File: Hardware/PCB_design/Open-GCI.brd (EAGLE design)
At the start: 100 x 94 mm, 29 parts, among them IC1 IC1, IC2 IC2, X1 USB

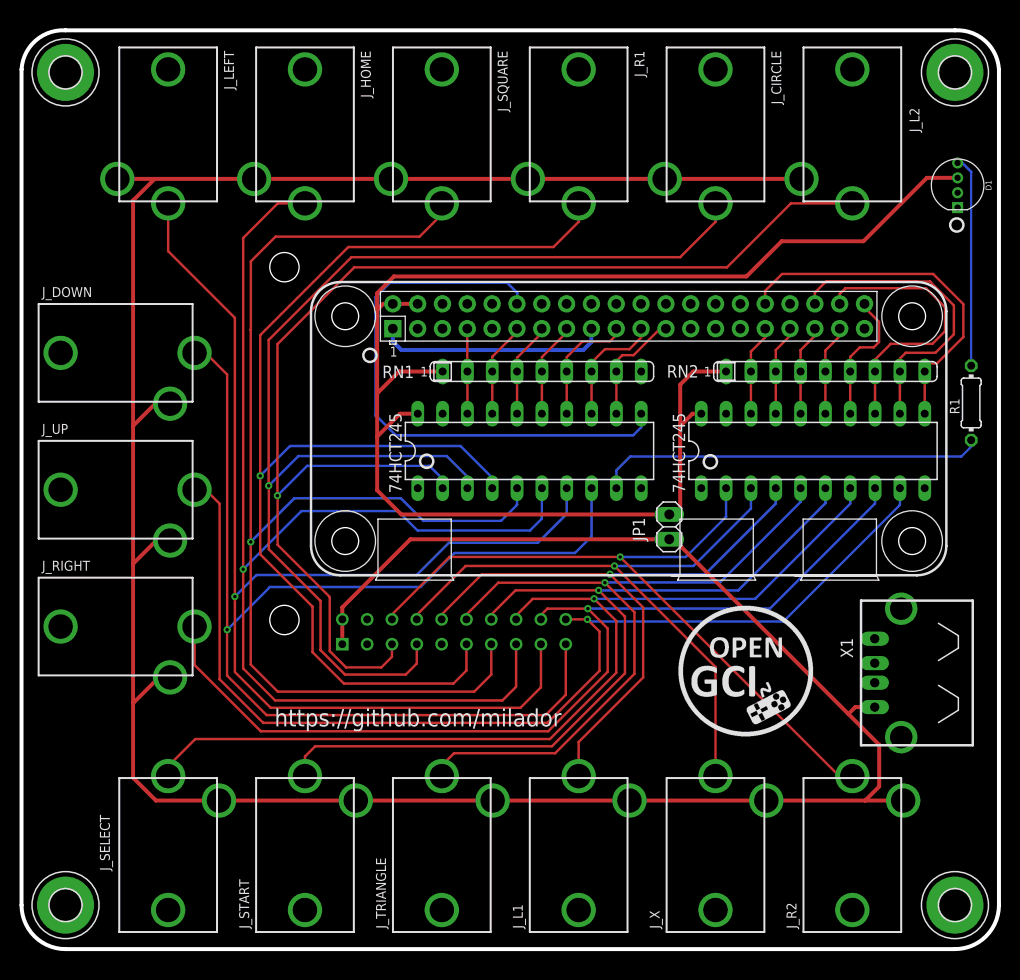
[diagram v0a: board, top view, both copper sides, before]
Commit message: Fixed the 3.5mm jack issue
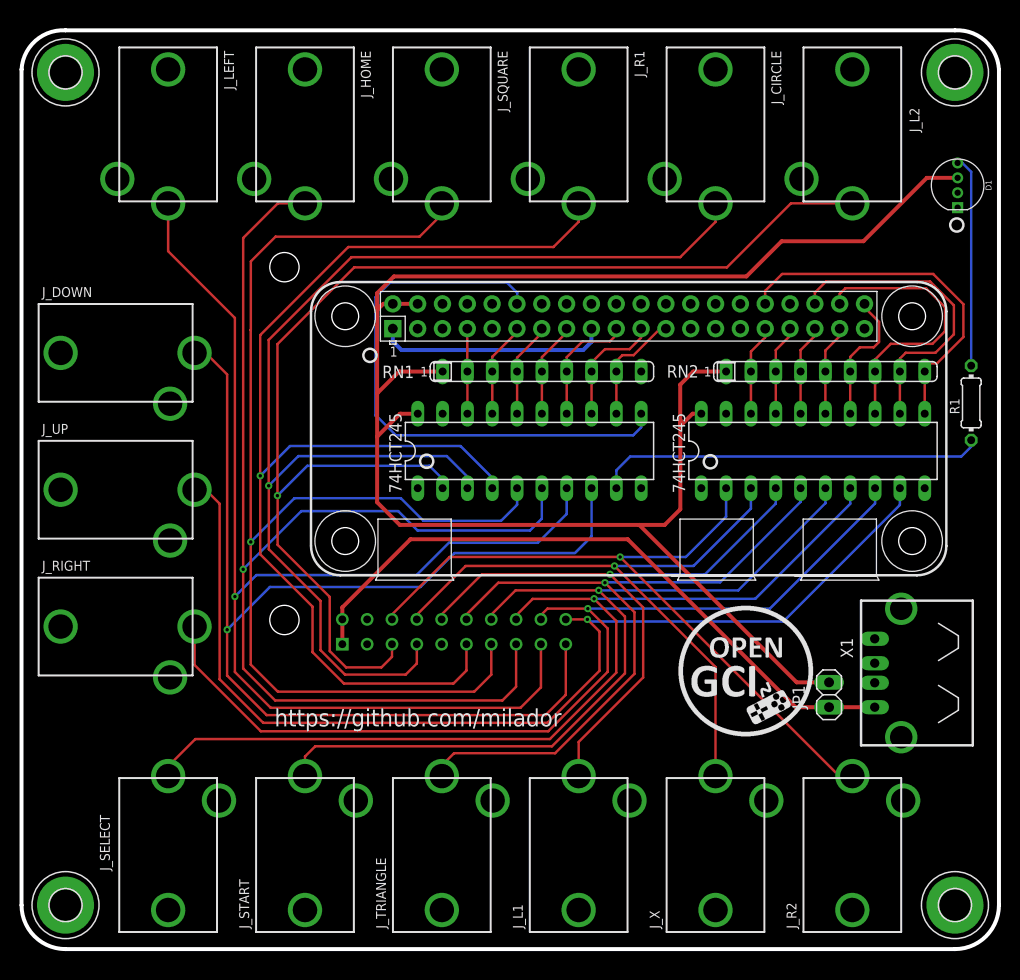
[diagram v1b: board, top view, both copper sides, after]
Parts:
- moved JP1 23.7 mm to (82.6, 26.0)
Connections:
- net +5V/2: no longer J_CIRCLE.3, J_DOWN.3, J_HOME.3, J_L1.3, J_L2.3, J_LEFT.3, J_R1.3, J_R2.3, J_RIGHT.3, J_SELECT.3, J_SQUARE.3, J_START.3, J_TRIANGLE.3, J_UP.3, J_X.3
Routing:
- net +5V/2: track 305.9 -> 68.2 mm
- net +5V: track 154.5 -> 182.9 mm
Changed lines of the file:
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@@
 <setting verticaltext="up"/>
 </settings>
-<grid distance="0.00999999999" unitdist="mm" unit="mm" style="lines" multiple="1" display="yes" altdistance="5" altunitdist="mil" altunit="mil"/>
+<grid distance="0.00196850394" unitdist="inch" unit="inch" style="lines" multiple="1" display="yes" altdistance="5" altunitdist="mil" altunit="mil"/>
 <layers>
 <layer number="1" name="Top" color="4" fill="1" visible="yes" active="yes"/>
@@
 <attribute name="OC_NEWARK" value="unknown" x="82.245" y="59.0945625" size="1.778" layer="27" display="off"/>
 </element>
-<element name="X1" library="open-gci-package" package="PN87520-S" package3d_urn="urn:adsk.eagle:package:6147/1" value="USB" x="90" y="28.255403125" smashed="yes" rot="R90">
-<attribute name="MF" value="" x="90" y="28.255403125" size="1.778" layer="27" rot="R90" display="off"/>
-<attribute name="MPN" value="" x="90" y="28.255403125" size="1.778" layer="27" rot="R90" display="off"/>
-<attribute name="NAME" x="85.07" y="29.775403125" size="1.27" layer="25" rot="R90"/>
-<attribute name="OC_FARNELL" value="unknown" x="90" y="28.255403125" size="1.778" layer="27" rot="R90" display="off"/>
-<attribute name="OC_NEWARK" value="unknown" x="90" y="28.255403125" size="1.778" layer="27" rot="R90" display="off"/>
-<attribute name="VALUE" x="90.980440625" y="30.06134375" size="1.27" layer="27" rot="R270"/>
+<element name="X1" library="open-gci-package" package="PN87520-S" package3d_urn="urn:adsk.eagle:package:6147/1" value="USB" x="90" y="28.25" smashed="yes" rot="R90">
+<attribute name="MF" value="" x="90" y="28.25" size="1.778" layer="27" rot="R90" display="off"/>
+<attribute name="MPN" value="" x="90" y="28.25" size="1.778" layer="27" rot="R90" display="off"/>
+<attribute name="NAME" x="85.07" y="29.77" size="1.27" layer="25" rot="R90"/>
+<attribute name="OC_FARNELL" value="unknown" x="90" y="28.25" size="1.778" layer="27" rot="R90" display="off"/>
+<attribute name="OC_NEWARK" value="unknown" x="90" y="28.25" size="1.778" layer="27" rot="R90" display="off"/>
+<attribute name="VALUE" x="90.980440625" y="30.055940625" size="1.27" layer="27" rot="R270"/>
 </element>
 <element name="D1" library="open-gci-package" package="NEOPIXEL-RGB-THRU" value="RGB LED" x="95.77196875" y="78.14690625" rot="R270"/>
@@
 <attribute name="VALUE" x="96.6774" y="56.8556" size="0.9906" layer="27" ratio="10" rot="R270"/>
 </element>
-<element name="JP1" library="pinhead" library_urn="urn:adsk.eagle:library:325" package="1X02" package3d_urn="urn:adsk.eagle:package:22435/2" value="No Rpi" x="66.27" y="43.2" smashed="yes" rot="R90">
-<attribute name="NAME" x="63.7912" y="41.7538" size="1.27" layer="25" ratio="10" rot="R90"/>
+<element name="JP1" library="pinhead" library_urn="urn:adsk.eagle:library:325" package="1X02" package3d_urn="urn:adsk.eagle:package:22435/2" value="No Rpi" x="82.62" y="26.02" smashed="yes" rot="R90">
+<attribute name="NAME" x="80.1412" y="24.5738" size="1.27" layer="25" ratio="10" rot="R90"/>
 </element>
 </elements>
@@
 <wire x1="36.381690625" y1="67.105528125" x2="36.381690625" y2="65.39103125" width="0.4064" layer="1"/>
 <wire x1="38.09619375" y1="68.82003125" x2="36.381690625" y2="67.105528125" width="0.4064" layer="1"/>
-<wire x1="36.381690625" y1="46.943009375" x2="36.381690625" y2="52.429409375" width="0.4064" layer="1"/>
 <contactref element="JP1" pad="2"/>
-<wire x1="66.27" y1="44.47" x2="38.8547" y2="44.47" width="0.4064" layer="1"/>
-<wire x1="38.8547" y1="44.47" x2="36.381690625" y2="46.943009375" width="0.4064" layer="1"/>
 <wire x1="72.085" y1="59.0945625" x2="68.7345625" y2="59.0945625" width="0.4064" layer="1"/>
 <wire x1="68.7345625" y1="59.0945625" x2="67.39" y2="57.75" width="0.4064" layer="1"/>
-<wire x1="67.39" y1="57.75" x2="67.39" y2="53.52" width="0.4064" layer="1"/>
-<wire x1="67.39" y1="53.52" x2="67.39" y2="45.02" width="0.4064" layer="1"/>
-<wire x1="66.84" y1="44.47" x2="66.27" y2="44.47" width="0.4064" layer="1"/>
-<wire x1="67.39" y1="45.02" x2="66.84" y2="44.47" width="0.4064" layer="1"/>
+<wire x1="67.39" y1="57.75" x2="67.39" y2="54.15" width="0.4064" layer="1"/>
+<wire x1="67.39" y1="54.15" x2="67.39" y2="53.52" width="0.4064" layer="1"/>
 <wire x1="69.5452" y1="54.7765625" x2="68.6465625" y2="54.7765625" width="0.4064" layer="1"/>
 <wire x1="68.6465625" y1="54.7765625" x2="67.39" y2="53.52" width="0.4064" layer="1"/>
+<wire x1="79.31" y1="27.29" x2="82.62" y2="27.29" width="0.4064" layer="1"/>
+<wire x1="36.381690625" y1="52.429409375" x2="36.381690625" y2="45.718309375" width="0.4064" layer="1"/>
+<wire x1="36.381690625" y1="45.718309375" x2="38.7" y2="43.4" width="0.4064" layer="1"/>
+<wire x1="38.7" y1="43.4" x2="63.2" y2="43.4" width="0.4064" layer="1"/>
+<wire x1="63.2" y1="43.4" x2="79.31" y2="27.29" width="0.4064" layer="1"/>
+<wire x1="63.2" y1="43.4" x2="65.8" y2="43.4" width="0.4064" layer="1"/>
+<wire x1="65.8" y1="43.4" x2="67.4" y2="45" width="0.4064" layer="1"/>
+<wire x1="67.4" y1="45" x2="67.4" y2="54.14" width="0.4064" layer="1"/>
+<wire x1="67.4" y1="54.14" x2="67.39" y2="54.15" width="0.4064" layer="1"/>
 </signal>
 <signal name="N$16">
@@
 <contactref element="U$2" pad="VCC2"/>
 <wire x1="32.82" y1="31.1945625" x2="32.82" y2="33.7345625" width="0.4064" layer="1"/>
-<contactref element="J_DOWN" pad="3"/>
-<contactref element="J_LEFT" pad="3"/>
-<contactref element="J_HOME" pad="3"/>
-<contactref element="J_L2" pad="3"/>
-<contactref element="J_CIRCLE" pad="3"/>
-<contactref element="J_SQUARE" pad="3"/>
-<contactref element="J_R1" pad="3"/>
-<wire x1="23.8" y1="78.8" x2="37.8" y2="78.8" width="0.4064" layer="1"/>
-<wire x1="79.8" y1="78.8" x2="65.8" y2="78.8" width="0.4064" layer="1"/>
-<wire x1="65.8" y1="78.8" x2="51.8" y2="78.8" width="0.4064" layer="1"/>
-<wire x1="51.8" y1="78.8" x2="37.8" y2="78.8" width="0.4064" layer="1"/>
-<contactref element="J_R2" pad="3"/>
-<contactref element="J_L1" pad="3"/>
-<contactref element="J_TRIANGLE" pad="3"/>
-<contactref element="J_SELECT" pad="3"/>
-<contactref element="J_RIGHT" pad="3"/>
-<contactref element="J_X" pad="3"/>
-<contactref element="J_START" pad="3"/>
-<contactref element="J_UP" pad="3"/>
-<wire x1="76.2" y1="15.2" x2="62.2" y2="15.2" width="0.4064" layer="1"/>
-<wire x1="62.2" y1="15.2" x2="48.2" y2="15.2" width="0.4064" layer="1"/>
-<wire x1="48.2" y1="15.2" x2="34.2" y2="15.2" width="0.4064" layer="1"/>
-<wire x1="34.2" y1="15.2" x2="20.2" y2="15.2" width="0.4064" layer="1"/>
-<wire x1="20.2" y1="15.2" x2="13.75" y2="15.2" width="0.4064" layer="1"/>
-<wire x1="13.75" y1="15.2" x2="11.41" y2="17.54" width="0.4064" layer="1"/>
-<wire x1="11.41" y1="17.54" x2="11.41" y2="25.15" width="0.4064" layer="1"/>
-<wire x1="11.41" y1="25.15" x2="14.06" y2="27.8" width="0.4064" layer="1"/>
-<wire x1="14.06" y1="27.8" x2="15.2" y2="27.8" width="0.4064" layer="1"/>
-<wire x1="15.2" y1="41.8" x2="13.79" y2="41.8" width="0.4064" layer="1"/>
-<wire x1="11.41" y1="39.42" x2="11.41" y2="25.15" width="0.4064" layer="1"/>
-<wire x1="13.79" y1="41.8" x2="11.41" y2="39.42" width="0.4064" layer="1"/>
-<wire x1="11.41" y1="53.53" x2="11.41" y2="39.42" width="0.4064" layer="1"/>
-<wire x1="13.68" y1="55.8" x2="11.41" y2="53.53" width="0.4064" layer="1"/>
-<wire x1="11.41" y1="76.5864" x2="11.41" y2="53.53" width="0.4064" layer="1"/>
-<wire x1="13.6236" y1="78.8" x2="11.41" y2="76.5864" width="0.4064" layer="1"/>
 <contactref element="X1" pad="1"/>
-<wire x1="86.31" y1="15.2" x2="76.2" y2="15.2" width="0.4064" layer="1"/>
-<wire x1="90.2" y1="15.2" x2="86.31" y2="15.2" width="0.4064" layer="1"/>
-<wire x1="23.8" y1="78.8" x2="13.6236" y2="78.8" width="0.4064" layer="1"/>
-<wire x1="9.8" y1="78.8" x2="13.6236" y2="78.8" width="0.4064" layer="1"/>
-<wire x1="15.2" y1="55.8" x2="13.68" y2="55.8" width="0.4064" layer="1"/>
 <contactref element="JP1" pad="1"/>
-<wire x1="66.27" y1="41.93" x2="39.79" y2="41.93" width="0.4064" layer="1"/>
 <wire x1="32.82" y1="34.96" x2="32.82" y2="33.7345625" width="0.4064" layer="1"/>
-<wire x1="39.79" y1="41.93" x2="32.82" y2="34.96" width="0.4064" layer="1"/>
-<wire x1="66.27" y1="41.93" x2="66.72" y2="41.93" width="0.4064" layer="1"/>
-<wire x1="87.75" y1="16.64" x2="86.31" y2="15.2" width="0.4064" layer="1"/>
-<wire x1="66.72" y1="41.93" x2="84.6" y2="24.05" width="0.4064" layer="1"/>
-<wire x1="84.6" y1="24.05" x2="87.75" y2="20.9" width="0.4064" layer="1"/>
-<wire x1="87.75" y1="20.9" x2="87.75" y2="16.64" width="0.4064" layer="1"/>
-<wire x1="87.29" y1="24.755403125" x2="85.305403125" y2="24.755403125" width="0.4064" layer="1"/>
-<wire x1="85.305403125" y1="24.755403125" x2="84.6" y2="24.05" width="0.4064" layer="1"/>
+<wire x1="32.82" y1="34.96" x2="39.79" y2="41.93" width="0.4064" layer="1"/>
+<wire x1="87.29" y1="24.75" x2="82.62" y2="24.75" width="0.4064" layer="1"/>
+<wire x1="39.79" y1="41.93" x2="62.02" y2="41.93" width="0.4064" layer="1"/>
+<wire x1="62.02" y1="41.93" x2="79.2" y2="24.75" width="0.4064" layer="1"/>
+<wire x1="79.2" y1="24.75" x2="82.62" y2="24.75" width="0.4064" layer="1"/>
 </signal>
 <signal name="N$32">

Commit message: Updated PCB, Component listand gerber files
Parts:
- removed D1: RGB LED, open-gci-package:NEOPIXEL-RGB-THRU
- removed U$1: RPI-ZERO, open-gci-package:RASPBERRYPI_BASTELSTUBE_V13_RASPI_BOARD_B+_FULL
- removed U$2: BROOK, open-gci-package:BROOK
- removed X1: USB, open-gci-package:PN87520-S
- added H5, H6, H7, H8: (no value), SparkFun-Hardware:STAND-OFF
- added JP2: RASPBERRYPI ZERO, milador:RASPBERRYPI_ZERO
- added JP3: BROOK, milador:CONN_2X10
- added L1: NEOPIXELS, milador:NEOPIXELS-5MM
- IC1: value IC1 -> SN74HCT245; device open-gci-package:74HCT245 -> milador:SN74HCT245
- IC2: value IC2 -> SN74HCT245; device open-gci-package:74HCT245 -> milador:SN74HCT245
- J_CIRCLE, J_DOWN, J_HOME, J_L1, J_L2, J_LEFT, J_R1, J_R2, J_RIGHT, J_SELECT, J_SQUARE, J_START, J_TRIANGLE, J_UP, J_X: value MJ-3536N -> SJ1-3535NG; device con-cuistack:MJ-3536N -> milador:CUI_SJ1-3535NG
- R1: device rcl:0204/7 -> milador:0204/7
- RN1, RN2: device resistor-sil:SIL9 -> milador:SIL9
- moved J_X 87.3 mm to (55.0, 89.8), turned to 270 degrees
- moved J_TRIANGLE 85.9 mm to (45.0, 89.8), turned to 270 degrees
- moved J_LEFT 85.8 mm to (14.7, 4.16), turned to 90 degrees
- moved J_R2 85.8 mm to (85.3, 89.8), turned to 270 degrees
- moved JP1 78.6 mm to (7.99, 50.5)
- moved J_DOWN 60.6 mm to (24.8, 4.11), turned to 90 degrees
- moved R1 55.7 mm to (44.5, 37.8), turned to 180 degrees
- moved J_UP 52.7 mm to (34.9, 4.31), turned to 90 degrees
- moved J_RIGHT 50.0 mm to (45.0, 4.36), turned to 90 degrees
- moved J_SELECT 40.1 mm to (55.0, 4.46), turned to 90 degrees
- moved J_START 36.2 mm to (65.2, 4.46), turned to 90 degrees
- moved J_CIRCLE 36.2 mm to (34.9, 89.8), turned to 270 degrees
- moved IC1 19.5 mm to (33.0, 46.3), turned to 90 degrees
- moved IC2 19.5 mm to (62.1, 46.3), turned to 90 degrees
- moved RN1 19.5 mm to (34.3, 54.4)
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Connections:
- removed net N$1: IC1.A0, J_L2.2, U$2.L2
- removed net N$10: IC2.A2, J_L1.2, U$2.L1
- removed net N$11: IC2.A3, J_TRIANGLE.2, U$2.TRIANGLE
- removed net N$12: IC2.A4, J_START.2, U$2.START
- removed net N$13: IC2.A5, J_SELECT.2, U$2.SELECT
- removed net N$14: IC2.A6, J_RIGHT.2, U$2.RIGHT
- removed net N$15: IC2.A7, J_UP.2, U$2.UP
- removed net N$16: IC1.B0, RN1.2, U$1.7
- removed net N$17: IC1.B1, RN1.3, U$1.11
- removed net N$18: IC1.B2, RN1.4, U$1.13
- removed net N$19: IC1.B3, RN1.5, U$1.15
- removed net N$2: IC1.A1, J_CIRCLE.2, U$2.CIRCLE
- removed net N$20: IC1.B5, RN1.7, U$1.21
- removed net N$21: IC1.B4, RN1.6, U$1.19
- removed net N$22: IC1.B6, RN1.8, U$1.23
- removed net N$23: IC1.B7, U$1.12
- removed net N$24: IC2.B1, RN2.3, U$1.33
- removed net N$25: IC2.B0, RN2.2, U$1.31
- removed net N$26: IC2.B2, RN2.4, U$1.35
- removed net N$27: IC2.B3, RN2.5, U$1.37
- removed net N$28: IC2.B4, RN2.6, U$1.40
- removed net N$29: IC2.B5, RN2.7, U$1.38
- removed net N$3: IC1.A2, J_R1.2, U$2.R1
- removed net N$30: IC2.B6, RN2.8, U$1.36
- removed net N$31: IC2.B7, RN2.9, U$1.32
- removed net N$4: IC1.A3, J_SQUARE.2, U$2.SQUARE
- removed net N$5: IC1.A4, J_HOME.2, U$2.HOME
- removed net N$6: IC1.A5, J_LEFT.2, U$2.LEFT
- removed net N$7: IC1.A6, J_DOWN.2, U$2.DOWN
- removed net N$8: IC2.A0, J_R2.2, U$2.R2
- removed net N$9: IC2.A1, J_X.2, U$2.X
- new net NGP11: IC1.17, JP2.11, RN1.3
- new net NGP12: IC1.11, JP2.12
- new net NGP13: IC1.16, JP2.13, RN1.4
- new net NGP15: IC1.15, JP2.15, RN1.5
- new net NGP19: IC1.14, JP2.19, RN1.6
- new net NGP21: IC1.13, JP2.21, RN1.7
- new net NGP23: IC1.12, JP2.23, RN1.8
- new net NGP31: IC2.18, JP2.31, RN2.2
- new net NGP32: IC2.11, JP2.32, RN2.9
- new net NGP33: IC2.17, JP2.33, RN2.3
- new net NGP35: IC2.16, JP2.35, RN2.4
- new net NGP36: IC2.12, JP2.36, RN2.8
- new net NGP37: IC2.15, JP2.37, RN2.5
- new net NGP38: IC2.13, JP2.38, RN2.7
- new net NGP40: IC2.14, JP2.40, RN2.6
- new net NGP7: IC1.18, JP2.7, RN1.2
- new net NJ_CIR: IC1.3, JP3.CIRCLE, J_CIRCLE.2
- new net NJ_DOWN: IC1.8, JP3.DOWN, J_DOWN.2
- new net NJ_HOME: IC1.6, JP3.HOME, J_HOME.2
- new net NJ_L1: IC2.4, JP3.L1, J_L1.2
- new net NJ_L2: IC1.2, JP3.L2, J_L2.2
- new net NJ_LEFT: IC1.7, JP3.LEFT, J_LEFT.2
- new net NJ_R1: IC1.4, JP3.R1, J_R1.2
- new net NJ_R2: IC2.2, JP3.R2, J_R2.2
- new net NJ_RIGHT: IC2.8, JP3.RIGHT, J_RIGHT.2
- new net NJ_SELECT: IC2.7, JP3.SELECT, J_SELECT.2
- new net NJ_SQU: IC1.5, JP3.SQUARE, J_SQUARE.2
- new net NJ_START: IC2.6, JP3.START, J_START.2
- new net NJ_TRI: IC2.5, JP3.TRIANGLE, J_TRIANGLE.2
- new net NJ_UP: IC2.9, JP3.UP, J_UP.2
- new net NJ_X: IC2.3, JP3.X, J_X.2
- net +3V3: now also JP2.1, JP2.17; no longer U$1.1, U$1.17
- net +5V: now also IC1.20, IC2.20, JP2.2, JP2.4, L1.2; no longer D1.3, IC1.VCC, IC2.VCC, U$1.2, U$1.4
- net +5V/2: now also JP3.VCC1, JP3.VCC2; no longer U$2.VCC1, U$2.VCC2, X1.1
- net GND: now also IC1.1, IC1.10, IC1.19, IC2.1, IC2.10, IC2.19, JP2.14, JP2.20, JP2.25, JP2.30, JP2.34, JP2.39, JP2.6, JP2.9, JP3.GND1, JP3.GND2, JP3.GND3, L1.3, L1.4; no longer D1.1, D1.2, IC1.DIR, IC1.GND, IC1.OE, IC2.DIR, IC2.GND, IC2.OE, U$1.14, U$1.20, U$1.25, U$1.30, U$1.34, U$1.39, U$1.6, U$1.9, U$2.GND1, U$2.GND2, U$2.GND3, X1.2, X1.3, X1.4, X1.S1, X1.S2
- net N$32: now also IC1.9; no longer IC1.A7
- net N$33: now also L1.1; no longer D1.4
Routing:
- net NJ_R1: track 0.00 -> 184.5 mm, vias 0 -> 1
- net NJ_L2: track 0.00 -> 167.5 mm, vias 0 -> 1
- net NJ_HOME: track 0.00 -> 151.4 mm, vias 0 -> 1
- net NJ_X: track 0.00 -> 149.9 mm, vias 0 -> 1
- net NJ_SQU: track 0.00 -> 148.6 mm, vias 0 -> 1
- net NJ_CIR: track 0.00 -> 143.7 mm, vias 0 -> 1
- net N$6: track 129.0 -> 0.00 mm, vias 1 -> 0
- net N$1: track 126.9 -> 0.00 mm, vias 1 -> 0
- net NJ_TRI: track 0.00 -> 126.3 mm, vias 0 -> 2
- net N$4: track 126.0 -> 0.00 mm, vias 1 -> 0
- net N$7: track 123.6 -> 0.00 mm, vias 1 -> 0
- net N$2: track 123.6 -> 0.00 mm, vias 1 -> 0
- net N$5: track 123.5 -> 0.00 mm, vias 1 -> 0
- net N$3: track 121.7 -> 0.00 mm, vias 1 -> 0
- net NJ_R2: track 0.00 -> 113.8 mm, vias 0 -> 1
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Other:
- outline, holes or cut-outs redrawn
- board text added: "USB Powered"
- board text added: "V 1.1"
- board text added: "https://github.com/milador/Open-GCI"
- board text removed: "https://github.com/milador"
